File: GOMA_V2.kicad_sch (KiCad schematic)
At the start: 83 parts, among them J1 AudioJack2_SwitchT, J10 AudioJack2_SwitchT, J11 AudioJack2_SwitchT, J12 Conn_01x08_Pin, J13 Conn_01x08_Socket, J14 AudioJack2_SwitchT, J15 AudioJack2_SwitchT, J16 Conn_01x08_Pin, J17 Conn_01x08_Socket, J18 Conn_02x05_Odd_Even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

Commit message: v3 design start
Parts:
- added C10, C4, C7, C8, C9: 100n, Capacitor_THT:C_Disc_D6.0mm_W2.5mm_P5.00mm, symbol Device:C
- J1: value AudioJack2_SwitchT -> ch1 in
- J10: value AudioJack2_SwitchT -> ch3 in
- J11: value AudioJack2_SwitchT -> ch3 out
- J14: value AudioJack2_SwitchT -> ch4 in
- J15: value AudioJack2_SwitchT -> ch4 out
- J2: value AudioJack2_SwitchT -> ch1 out
- J4: value AudioJack2_SwitchT -> ch2 in
- J5: value AudioJack2_SwitchT -> ch2 out
- R10, R20, R21, R31, R32, R42, R43, R6: footprint Resistor_THT:R_Axial_DIN0207_L6.3mm_D2.5mm_P10.16mm_Horizontal -> Resistor_THT:R_Axial_DIN0207_L6.3mm_D2.5mm_P2.54mm_Vertical
- SW1, SW2, SW3, SW4: footprint Custom:SMTS 102 SPDT -> Custom:SMTS 102 SPDT PCB
- renumbered C4 to C6
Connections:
- net GND_FP.2 is gone; now on net GND_FP: J4.S, J5.S, J8.3 (Pin_3), R12.1, R22.1, RV2.1
- net GND_FP.3 is gone; now on net GND_FP: J10.S, J11.S, J12.3 (Pin_3), R23.1, R33.1, RV3.1
- net GND_FP.4 is gone; now on net GND_FP: J14.S, J15.S, J16.3 (Pin_3), R34.1, R44.1, RV4.1
- net +12V: now also J17.8 (Pin_8), C4.1; no longer U6.3 (VI)
- net +5V: no longer J13.8 (Pin_8), J17.8 (Pin_8), J7.8 (Pin_8), J9.8 (Pin_8), U6.1 (VO)
- net -12V: now also C10.2, C7.2, C8.2, C9.2; no longer C1.2, C2.2, C3.2
- net GND: now also C1.2, C2.2, C3.2, C10.1, C4.2, C7.1, C8.1, C9.1; no longer U6.2 (GND)
- net R10_BP: now also R10.1; no longer R10.2
- net R21_BP: now also R21.1; no longer R21.2
- net R32_BP: now also R32.1; no longer R32.2
- net R43_BP: now also R43.1; no longer R43.2
- net at R4.2, U1.14, U1.3 (+): now also R10.2; no longer R10.1
- net at R26.2, U3.14, U3.3 (+): now also R32.2; no longer R32.1
- net at R15.2, U2.14, U2.3 (+): now also R21.2; no longer R21.1
- net at R37.2, U4.14, U4.3 (+): now also R43.2; no longer R43.1
- net +5V_FP.1: no longer names the net of J6.8 (Pin_8)
- net +5V_FP.1: no longer J1.TN
- net +5V_FP.2: no longer names the net of J8.8 (Pin_8)
- net +5V_FP.2: no longer J4.TN
- net +5V_FP.3: no longer names the net of J12.8 (Pin_8)
- net +5V_FP.3: no longer J10.TN
- net +5V_FP.4 renamed +12V_FP
- net +12V_FP: now also U6.3 (VI); no longer J14.TN
- net GND_FP.1 renamed GND_FP
- net GND_FP: now also U6.2 (GND)
- new net +5V_FP: J1.TN, J10.TN, J14.TN, J4.TN, U6.1 (VO)
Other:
- moved on the sheet: C1, C2, C3, R10, R21, R32, R43

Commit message: bottom PCB routing
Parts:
- removed J12, J6, J8: Conn_01x08_Pin, Connector_PinHeader_2.54mm:PinHeader_1x08_P2.54mm_Vertical, symbol Connector:Conn_01x08_Pin
- removed J13, J7, J9: Conn_01x08_Socket, Connector_PinSocket_2.54mm:PinSocket_1x08_P2.54mm_Vertical, symbol Connector:Conn_01x08_Socket
- added J12, J6, J8: Conn_01x07_Pin, Connector_PinHeader_2.54mm:PinHeader_1x07_P2.54mm_Vertical, symbol Connector:Conn_01x07_Pin
- added J13, J7, J9: Conn_01x07_Socket, Connector_PinSocket_2.54mm:PinSocket_1x07_P2.54mm_Vertical, symbol Connector:Conn_01x07_Socket
- added J19: Daisy out, Connector_PinHeader_2.54mm:PinHeader_1x01_P2.54mm_Vertical, symbol Connector:Conn_01x01_Pin
- added J3: Daisy in, Connector_PinHeader_2.54mm:PinHeader_1x01_P2.54mm_Vertical, symbol Connector:Conn_01x01_Pin
- J18: footprint Connector_PinHeader_2.54mm:PinHeader_2x05_P2.54mm_Vertical -> Connector_IDC:IDC-Header_2x05_P2.54mm_Vertical
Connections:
- net GND: now also J17.2 (Pin_2), J13.7 (Pin_7), J7.3 (Pin_3), J9.7 (Pin_7); no longer J17.3 (Pin_3)
- net GND_FP: now also J16.2 (Pin_2), J12.7 (Pin_7), J6.3 (Pin_3), J8.7 (Pin_7); no longer J16.3 (Pin_3)
- net R10_BP: now also J7.2 (Pin_2)
- net R10_FP: now also J6.2 (Pin_2)
- net R11_BP: now also J7.1 (Pin_1)
- net R11_FP: now also J6.1 (Pin_1)
- net R17_BP: now also J9.1 (Pin_1)
- net R17_FP: now also J8.1 (Pin_1)
- net R21_BP: now also J9.2 (Pin_2)
- net R21_FP: now also J8.2 (Pin_2)
- net R28_BP: now also J13.1 (Pin_1)
- net R28_FP: now also J12.1 (Pin_1)
- net R32_BP: now also J13.2 (Pin_2)
- net R32_FP: now also J12.2 (Pin_2)
- net R43_BP: now also J17.3 (Pin_3); no longer J17.2 (Pin_2)
- net R43_FP: now also J16.3 (Pin_3); no longer J16.2 (Pin_2)
- net U1.1_BP: now also J7.4 (Pin_4)
- net U1.1_FP: now also J6.4 (Pin_4)
- net U1.2_BP: now also J7.5 (Pin_5)
- net U1.2_FP: now also J6.5 (Pin_5)
- net U1.5_BP: now also J7.6 (Pin_6)
- net U1.5_FP: now also R8.2, J6.6 (Pin_6); no longer R8.1
- net U1.6_BP: now also J7.7 (Pin_7)
- net U1.6_FP: now also J6.7 (Pin_7)
- net U2.1_BP: now also J9.6 (Pin_6)
- net U2.1_FP: now also J8.6 (Pin_6)
- net U2.2_BP: now also J9.5 (Pin_5)
- net U2.2_FP: now also J8.5 (Pin_5)
- net U2.5_BP: now also J9.4 (Pin_4)
- net U2.5_FP: now also R19.2, J8.4 (Pin_4); no longer R19.1
- net U2.6_BP: now also J9.3 (Pin_3)
- net U2.6_FP: now also J8.3 (Pin_3)
- net U3.1_BP: now also J13.3 (Pin_3)
- net U3.1_FP: now also J12.3 (Pin_3)
- net U3.2_BP: now also J13.4 (Pin_4)
- net U3.2_FP: now also J12.4 (Pin_4)
- net U3.5_BP: now also J13.5 (Pin_5)
- net U3.5_FP: now also R30.2, J12.5 (Pin_5); no longer R30.1
- net U3.6_BP: now also J13.6 (Pin_6)
- net U3.6_FP: now also J12.6 (Pin_6)
- net U4.1_BP: now also J17.4 (Pin_4); no longer J17.6 (Pin_6)
- net U4.1_FP: now also J16.4 (Pin_4); no longer J16.6 (Pin_6)
- net U4.5_BP: now also J17.6 (Pin_6); no longer J17.4 (Pin_4)
- net U4.5_FP: now also J16.6 (Pin_6), R41.2; no longer J16.4 (Pin_4), R41.1
- net at J1.T, RV1.3, SW1.1 (A): now also R8.1; no longer R8.2
- net at J10.T, RV3.3, SW3.1 (A): now also R30.1; no longer R30.2
- net at J14.T, RV4.3, SW4.1 (A): now also R41.1; no longer R41.2
- net at J4.T, RV2.3, SW2.1 (A): now also R19.1; no longer R19.2
- net Daisy chain in: no longer names the net of R3.1, R5.2, U1.9 (-)
- net Daisy chain in: now also J3.1 (Pin_1)
- net Daisy chain out: no longer names the net of R39.1
- net Daisy chain out: now also J19.1 (Pin_1)
- no-connect marks 1 -> 0
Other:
- moved on the sheet: J16, J17, R19, R30, R41, R8

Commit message: routing complete, DRC passes
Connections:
- net +12V: now also J17.1 (Pin_1); no longer J17.8 (Pin_8)
- net +12V_FP: now also J16.1 (Pin_1); no longer J16.8 (Pin_8)
- net R39_BP: now also J17.8 (Pin_8); no longer J17.1 (Pin_1)
- net R39_FP: now also J16.8 (Pin_8); no longer J16.1 (Pin_1)
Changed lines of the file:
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@@
 		)
 	)
+	(global_label "R39_FP"
+		(shape bidirectional)
+		(at 52.07 377.19 0)
+		(fields_autoplaced yes)
+		(effects
+			(font
+				(size 1.27 1.27)
+			)
+			(justify left)
+		)
+		(property "Intersheetrefs" "${INTERSHEET_REFS}"
+			(at 63.1817 377.19 0)
+			(effects
+				(font
+					(size 1.27 1.27)
+				)
+				(justify left)
+				(hide yes)
+			)
+		)
+	)
 	(global_label "R17_BP"
 		(shape bidirectional)
@@
 		)
 	)
-	(global_label "R39_FP"
-		(shape bidirectional)
-		(at 52.07 359.41 0)
-		(fields_autoplaced yes)
-		(effects
-			(font
-				(size 1.27 1.27)
-			)
-			(justify left)
-		)
-		(property "Intersheetrefs" "${INTERSHEET_REFS}"
-			(at 63.1817 359.41 0)
-			(effects
-				(font
-					(size 1.27 1.27)
-				)
-				(justify left)
-				(hide yes)
-			)
-		)
-	)
 	(global_label "U4.5_BP"
 		(shape bidirectional)
@@
 		)
 	)
+	(global_label "R39_BP"
+		(shape bidirectional)
+		(at 41.91 377.19 180)
+		(fields_autoplaced yes)
+		(effects
+			(font
+				(size 1.27 1.27)
+			)
+			(justify right)
+		)
+		(property "Intersheetrefs" "${INTERSHEET_REFS}"
+			(at 34.1245 377.19 0)
+			(effects
+				(font
+					(size 1.27 1.27)
+				)
+				(justify right)
+				(hide yes)
+			)
+		)
+	)
 	(global_label "R10_FP"
 		(shape bidirectional)
@@
 		)
 	)
-	(global_label "R39_BP"
-		(shape bidirectional)
-		(at 41.91 359.41 180)
-		(fields_autoplaced yes)
-		(effects
-			(font
-				(size 1.27 1.27)
-			)
-			(justify right)
-		)
-		(property "Intersheetrefs" "${INTERSHEET_REFS}"
-			(at 34.1245 359.41 0)
-			(effects
-				(font
-					(size 1.27 1.27)
-				)
-				(justify right)
-				(hide yes)
-			)
-		)
-	)
 	(global_label "U1.1_FP"
 		(shape bidirectional)
@@
 	(symbol
 		(lib_id "power:+5V")
-		(at 52.07 377.19 270)
+		(at 52.07 359.41 270)
 		(unit 1)
 		(exclude_from_sim no)
@@
 		(dnp no)
 		(property "Reference" "#PWR067"
-			(at 48.26 377.19 0)
+			(at 48.26 359.41 0)
 			(effects
 				(font
@@
 		)
 		(property "Value" "+12V_FP"
-			(at 55.88 377.1899 90)
+			(at 55.88 359.4099 90)
 			(effects
 				(font
@@
 		)
 		(property "Footprint" ""
-			(at 52.07 377.19 0)
+			(at 52.07 359.41 0)
 			(effects
 				(font
@@
 		)
 		(property "Datasheet" ""
-			(at 52.07 377.19 0)
+			(at 52.07 359.41 0)
 			(effects
 				(font
@@
 		)
 		(property "Description" "Power symbol creates a global label with name \"+5V\""
-			(at 52.07 377.19 0)
+			(at 52.07 359.41 0)
 			(effects
 				(font
@@
 		)
 		(instances
-			(project "GOMA"
+			(project "GOMA_V2"
 				(path "/96da86e7-a50f-451f-8b60-e0d897c8bc3d"
 					(reference "#PWR067")
@@
 	(symbol
 		(lib_id "power:+5V")
-		(at 41.91 377.19 90)
+		(at 41.91 359.41 90)
 		(mirror x)
 		(unit 1)
@@
 		(dnp no)
 		(property "Reference" "#PWR068"
-			(at 45.72 377.19 0)
+			(at 45.72 359.41 0)
 			(effects
 				(font
@@
 		)
 		(property "Value" "+12V"
-			(at 38.1 377.1899 90)
+			(at 38.1 359.4099 90)
 			(effects
 				(font
@@
 		)
 		(property "Footprint" ""
-			(at 41.91 377.19 0)
+			(at 41.91 359.41 0)
 			(effects
 				(font
@@
 		)
 		(property "Datasheet" ""
-			(at 41.91 377.19 0)
+			(at 41.91 359.41 0)
 			(effects
 				(font
@@
 		)
 		(property "Description" "Power symbol creates a global label with name \"+5V\""
-			(at 41.91 377.19 0)
+			(at 41.91 359.41 0)
 			(effects
 				(font
@@
 		)
 		(instances
-			(project "GOMA"
+			(project "GOMA_V2"
 				(path "/96da86e7-a50f-451f-8b60-e0d897c8bc3d"
 					(reference "#PWR068")

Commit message: adjusted component positioning
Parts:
- RV1, RV2, RV3, RV4: footprint Potentiometer_THT:Potentiometer_Alpha_RD901F-40-00D_Single_Vertical -> Custom:Potentiometer_Alpha_RD901F-40-00D_Single_Vertical_3D
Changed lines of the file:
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@@
 			)
 		)
-		(property "Footprint" "Potentiometer_THT:Potentiometer_Alpha_RD901F-40-00D_Single_Vertical"
+		(property "Footprint" "Custom:Potentiometer_Alpha_RD901F-40-00D_Single_Vertical_3D"
 			(at 68.58 63.5 0)
 			(effects
@@
 			)
 		)
-		(property "Footprint" "Potentiometer_THT:Potentiometer_Alpha_RD901F-40-00D_Single_Vertical"
+		(property "Footprint" "Custom:Potentiometer_Alpha_RD901F-40-00D_Single_Vertical_3D"
 			(at 69.85 142.24 0)
 			(effects
@@
 			)
 		)
-		(property "Footprint" "Potentiometer_THT:Potentiometer_Alpha_RD901F-40-00D_Single_Vertical"
+		(property "Footprint" "Custom:Potentiometer_Alpha_RD901F-40-00D_Single_Vertical_3D"
 			(at 66.04 330.2 0)
 			(effects
@@
 			)
 		)
-		(property "Footprint" "Potentiometer_THT:Potentiometer_Alpha_RD901F-40-00D_Single_Vertical"
+		(property "Footprint" "Custom:Potentiometer_Alpha_RD901F-40-00D_Single_Vertical_3D"
 			(at 67.31 240.03 0)
 			(effects

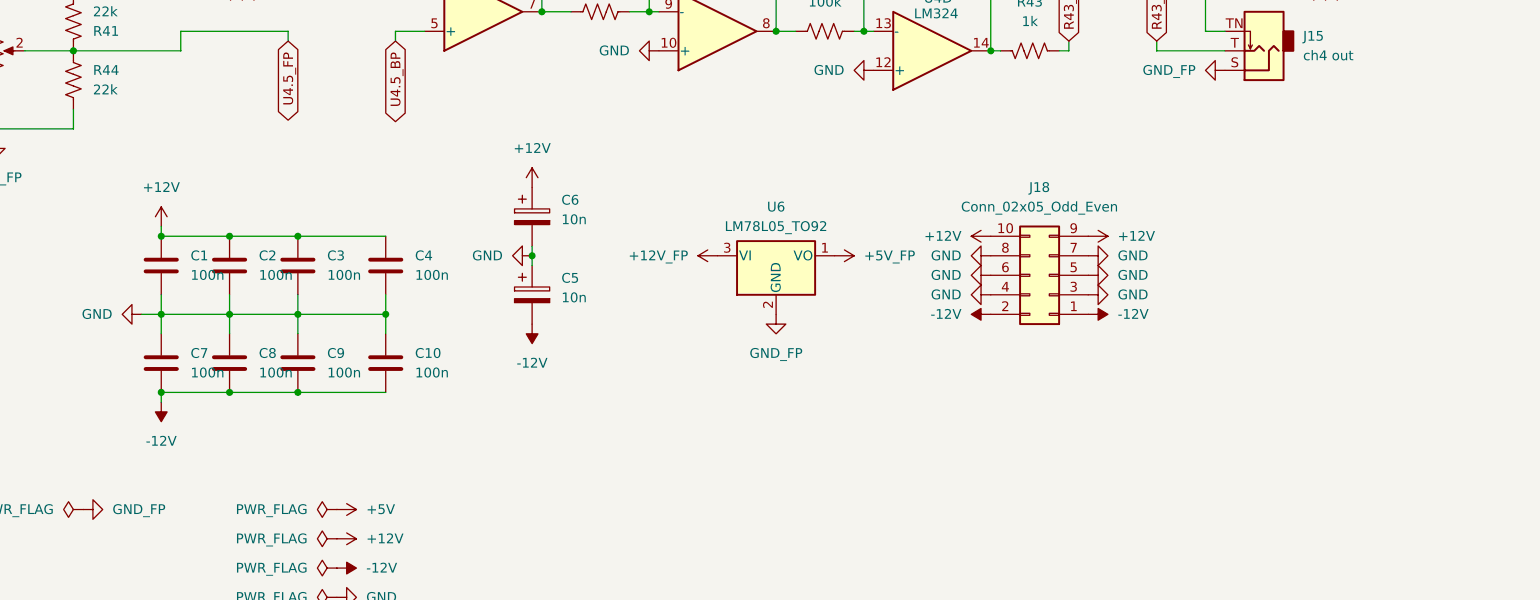
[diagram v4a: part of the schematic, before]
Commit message: Added voltage testpoints, front ground fill
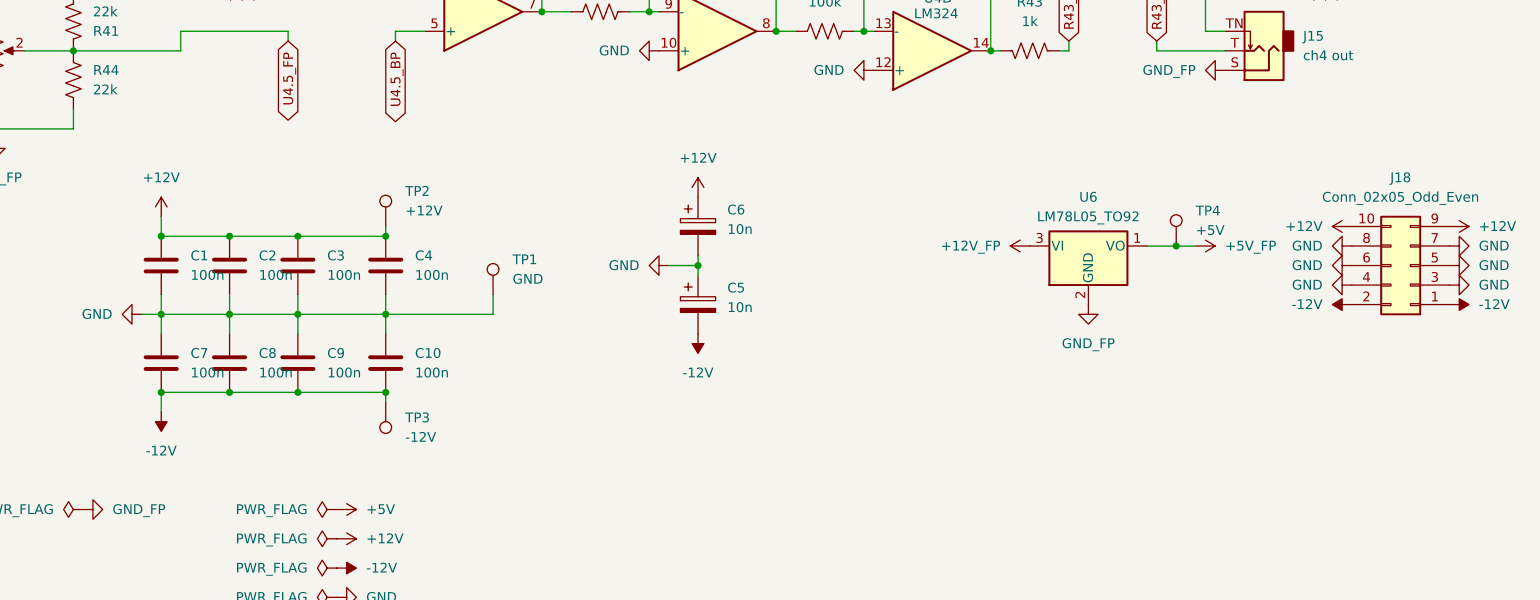
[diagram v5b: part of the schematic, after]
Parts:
- added TP1: GND, PCM_4ms_TestPoint:TestPoint_Pad_04, symbol Connector:TestPoint
- added TP2: +12V, PCM_4ms_TestPoint:TestPoint_Pad_04, symbol Connector:TestPoint
- added TP3: -12V, PCM_4ms_TestPoint:TestPoint_Pad_04, symbol Connector:TestPoint
- added TP4: +5V, PCM_4ms_TestPoint:TestPoint_Pad_04, symbol Connector:TestPoint
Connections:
- net +12V: now also TP2.1
- net +5V_FP: now also TP4.1
- net -12V: now also TP3.1
- net GND: now also TP1.1
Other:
- moved on the sheet: C5, C6, J18, U6
